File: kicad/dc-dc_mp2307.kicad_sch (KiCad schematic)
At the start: 20 parts

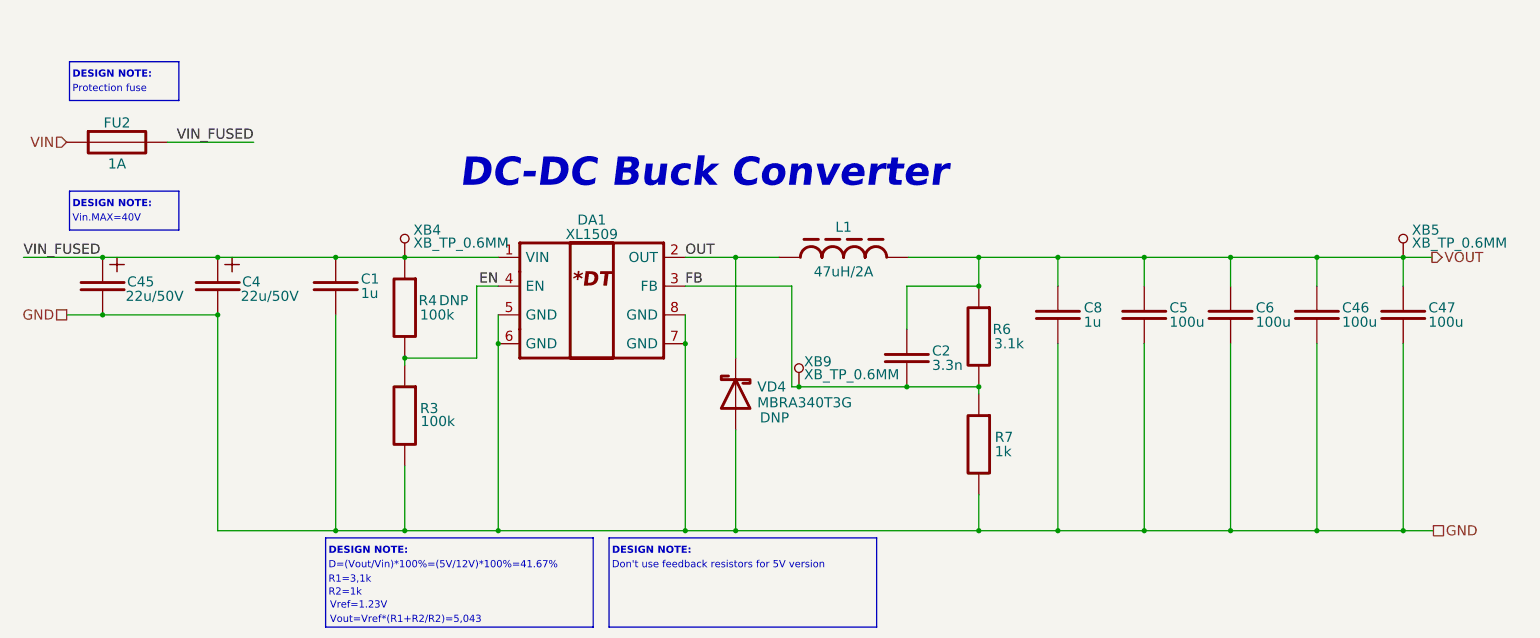
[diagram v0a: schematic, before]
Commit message: Reannotate schematic; Fix 5032 crystal footprint field; Update PCB with 5032 crystal
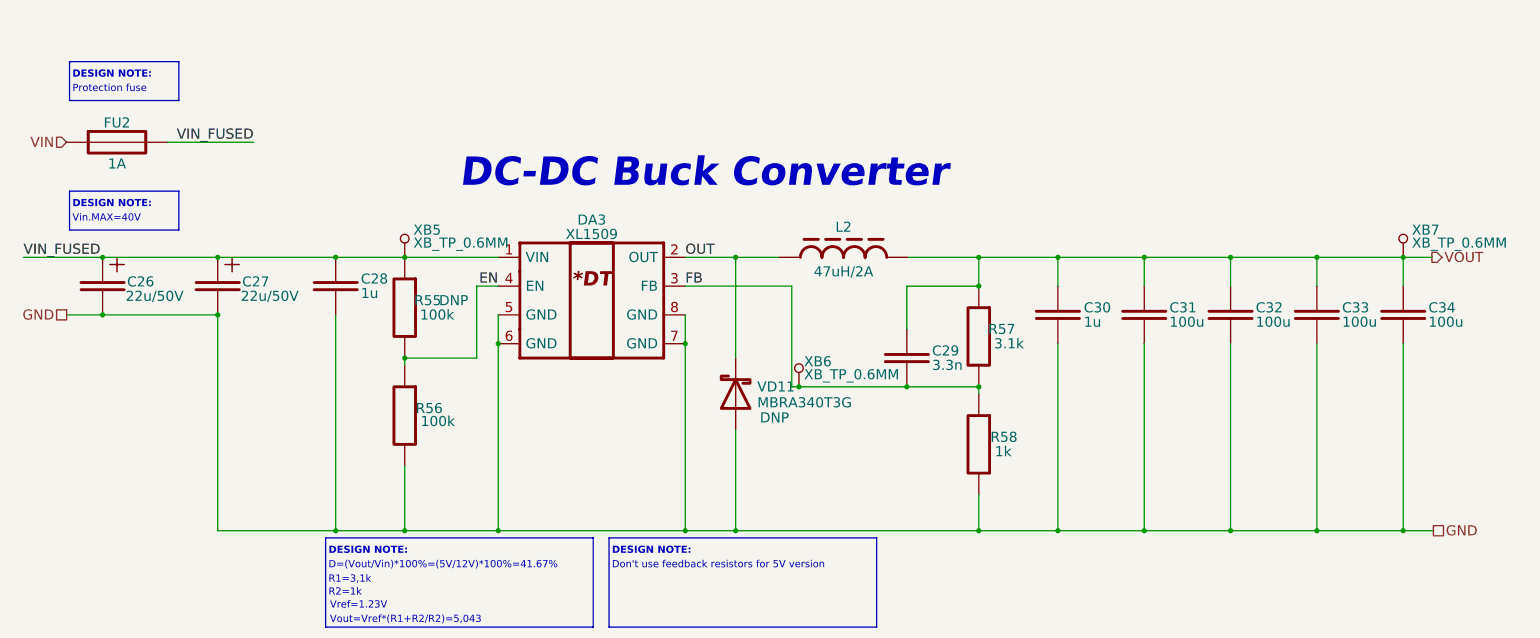
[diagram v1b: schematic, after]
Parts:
- renumbered C45 to C26, C4 to C27, C1 to C28, C2 to C29, C8 to C30, C5 to C31, C6 to C32, C46 to C33, C47 to C34, DA1 to DA3, L1 to L2, R4 to R55, R3 to R56, R6 to R57, R7 to R58, VD4 to VD11, XB4 to XB5, XB9 to XB6, XB5 to XB7
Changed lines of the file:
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@@
   (symbol (lib_id "Capacitors:C_CAP") (at 251.46 80.01 270) (unit 1)
     (in_bom yes) (on_board yes)
-    (property "Reference" "C46" (id 0) (at 255.905 78.74 90)
+    (property "Reference" "C33" (id 0) (at 255.905 78.74 90)
       (effects (font (size 1.778 1.778)) (justify left))
     )
@@
   (symbol (lib_id "Chips:XL1509") (at 123.444 77.47 0) (unit 1)
     (in_bom yes) (on_board yes)
-    (property "Reference" "DA1" (id 0) (at 123.444 63.246 0)
+    (property "Reference" "DA3" (id 0) (at 123.444 63.246 0)
       (effects (font (size 1.778 1.778)))
     )
@@
   (symbol (lib_id "Capacitors:C_CAP") (at 179.07 87.63 270) (unit 1)
     (in_bom yes) (on_board yes)
-    (property "Reference" "C2" (id 0) (at 183.515 86.36 90)
+    (property "Reference" "C29" (id 0) (at 183.515 86.36 90)
       (effects (font (size 1.778 1.778)) (justify left))
     )
@@
   (symbol (lib_id "Connectors:XB_TP_0.6MM") (at 160.0199 92.71 0) (unit 1)
     (in_bom no) (on_board yes)
-    (property "Reference" "XB9" (id 0) (at 160.909 88.265 0)
+    (property "Reference" "XB6" (id 0) (at 160.909 88.265 0)
       (effects (font (size 1.778 1.778)) (justify left))
     )
@@
   (symbol (lib_id "Diodes:VD_SCHOTTKY") (at 148.844 93.98 90) (unit 1)
     (in_bom yes) (on_board yes)
-    (property "Reference" "VD4" (id 0) (at 152.654 92.71 90)
+    (property "Reference" "VD11" (id 0) (at 152.654 92.71 90)
       (effects (font (size 1.778 1.778)) (justify right))
     )
@@
   (symbol (lib_id "Connectors:XB_TP_0.6MM") (at 266.7 69.85 0) (unit 1)
     (in_bom no) (on_board yes)
-    (property "Reference" "XB5" (id 0) (at 268.224 65.024 0)
+    (property "Reference" "XB7" (id 0) (at 268.224 65.024 0)
       (effects (font (size 1.778 1.778)) (justify left))
     )
@@
   (symbol (lib_id "Resistors:R_RES") (at 191.77 102.87 270) (unit 1)
     (in_bom yes) (on_board yes)
-    (property "Reference" "R7" (id 0) (at 196.215 101.6 90)
+    (property "Reference" "R58" (id 0) (at 196.215 101.6 90)
       (effects (font (size 1.778 1.778)))
     )
@@
   (symbol (lib_id "Resistors:R_RES") (at 90.424 78.74 270) (unit 1)
     (in_bom yes) (on_board yes)
-    (property "Reference" "R4" (id 0) (at 94.488 77.47 90)
+    (property "Reference" "R55" (id 0) (at 94.488 77.47 90)
       (effects (font (size 1.778 1.778)))
     )
@@
   (symbol (lib_id "Capacitors:C_CAP_PLUS") (at 57.404 74.93 270) (unit 1)
     (in_bom yes) (on_board yes)
-    (property "Reference" "C4" (id 0) (at 61.722 74.168 90)
+    (property "Reference" "C27" (id 0) (at 61.722 74.168 90)
       (effects (font (size 1.778 1.778)) (justify left))
     )
@@
   (symbol (lib_id "Capacitors:C_CAP") (at 220.98 80.01 270) (unit 1)
     (in_bom yes) (on_board yes)
-    (property "Reference" "C5" (id 0) (at 225.425 78.74 90)
+    (property "Reference" "C31" (id 0) (at 225.425 78.74 90)
       (effects (font (size 1.778 1.778)) (justify left))
     )
@@
   (symbol (lib_id "Capacitors:C_CAP") (at 78.232 74.93 270) (unit 1)
     (in_bom yes) (on_board yes)
-    (property "Reference" "C1" (id 0) (at 82.677 73.66 90)
+    (property "Reference" "C28" (id 0) (at 82.677 73.66 90)
       (effects (font (size 1.778 1.778)) (justify left))
     )
@@
   (symbol (lib_id "Capacitors:C_CAP") (at 266.7 80.01 270) (unit 1)
     (in_bom yes) (on_board yes)
-    (property "Reference" "C47" (id 0) (at 271.145 78.74 90)
+    (property "Reference" "C34" (id 0) (at 271.145 78.74 90)
       (effects (font (size 1.778 1.778)) (justify left))
     )
@@
   (symbol (lib_id "Capacitors:C_CAP_PLUS") (at 37.084 74.93 270) (unit 1)
     (in_bom yes) (on_board yes)
-    (property "Reference" "C45" (id 0) (at 41.402 74.168 90)
+    (property "Reference" "C26" (id 0) (at 41.402 74.168 90)
       (effects (font (size 1.778 1.778)) (justify left))
     )
@@
   (symbol (lib_id "Capacitors:C_CAP") (at 236.22 80.01 270) (unit 1)
     (in_bom yes) (on_board yes)
-    (property "Reference" "C6" (id 0) (at 240.665 78.74 90)
+    (property "Reference" "C32" (id 0) (at 240.665 78.74 90)
       (effects (font (size 1.778 1.778)) (justify left))
     )
@@
   (symbol (lib_id "Resistors:R_RES") (at 191.77 83.82 270) (unit 1)
     (in_bom yes) (on_board yes)
-    (property "Reference" "R6" (id 0) (at 195.834 82.55 90)
+    (property "Reference" "R57" (id 0) (at 195.834 82.55 90)
       (effects (font (size 1.778 1.778)))
     )
@@
   (symbol (lib_id "Inductors:L_DIEL") (at 167.894 69.85 0) (unit 1)
     (in_bom yes) (on_board yes)
-    (property "Reference" "L1" (id 0) (at 167.894 64.516 0)
+    (property "Reference" "L2" (id 0) (at 167.894 64.516 0)
       (effects (font (size 1.778 1.778)))
     )
@@
   (symbol (lib_id "Resistors:R_RES") (at 90.424 97.79 270) (unit 1)
     (in_bom yes) (on_board yes)
-    (property "Reference" "R3" (id 0) (at 94.742 96.52 90)
+    (property "Reference" "R56" (id 0) (at 94.742 96.52 90)
       (effects (font (size 1.778 1.778)))
     )
@@
   (symbol (lib_id "Capacitors:C_CAP") (at 205.74 80.01 270) (unit 1)
     (in_bom yes) (on_board yes)
-    (property "Reference" "C8" (id 0) (at 210.312 78.74 90)
+    (property "Reference" "C30" (id 0) (at 210.312 78.74 90)
       (effects (font (size 1.778 1.778)) (justify left))
     )
@@
   (symbol (lib_id "Connectors:XB_TP_0.6MM") (at 90.424 69.85 0) (unit 1)
     (in_bom no) (on_board yes)
-    (property "Reference" "XB4" (id 0) (at 91.948 65.024 0)
-      (effects (font (size 1.778 1.778)) (justify left))
-    )
+    (property "Reference" "XB5" (id 0) (at 91.948 65.024 0)
+      (effects (font (size 1.778 1.778)) (justify left))
+    )

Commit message: Add voltage value to caps, update BOM, SCH, ASM
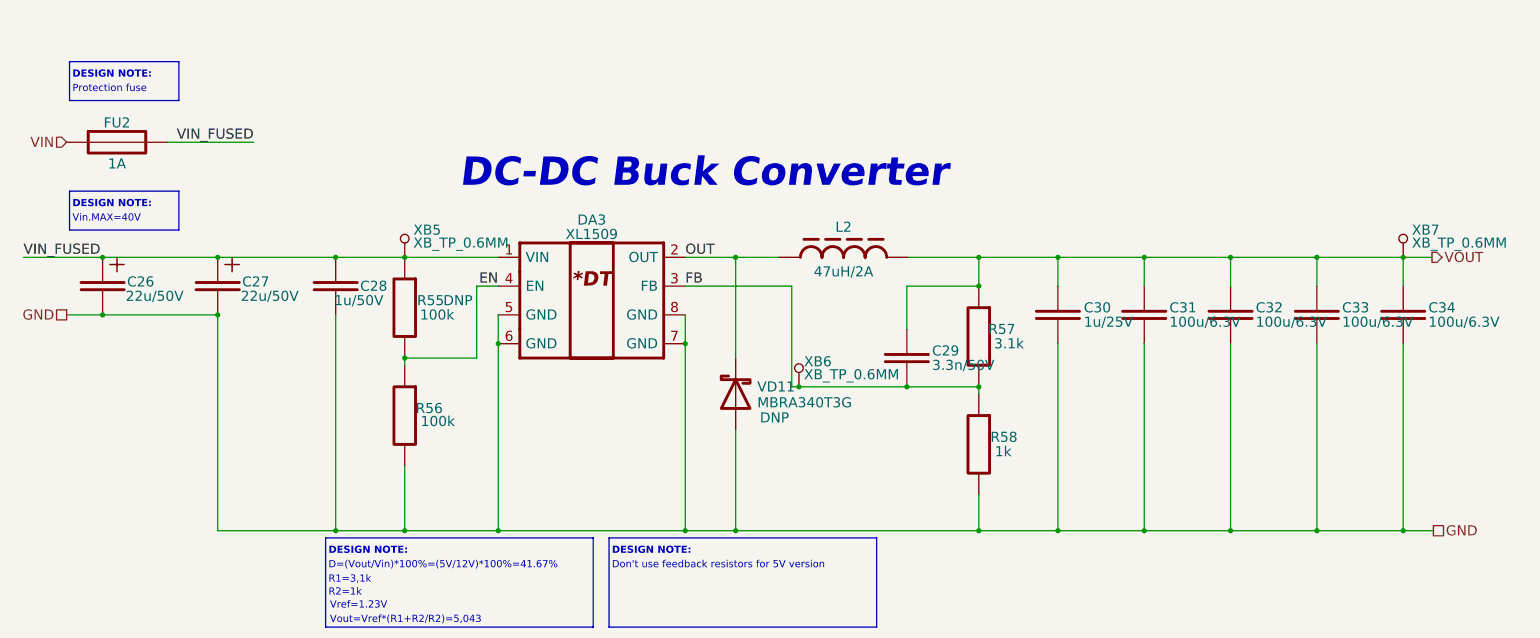
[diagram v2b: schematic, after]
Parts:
- C28: value 1u -> 1u/50V; Case/Package (none) -> 0805; Tolerance (none) -> ±10%; Type (none) -> X7R
- C29: value 3.3n -> 3.3n/50V; Case/Package (none) -> 1206; Tolerance (none) -> ±10%; Type (none) -> X7R
- C30: value 1u -> 1u/25V; Case/Package (none) -> 0603; Tolerance (none) -> ±10%; Type (none) -> X7R
- C31, C32, C33, C34: value 100u -> 100u/6.3V; Case/Package (none) -> 0603; Tolerance (none) -> ±10%; Type (none) -> X7R
- R55, R56: Case/Package 0000 -> 0603; Tolerance ±% -> ±5%
- R57: Case/Package 0000 -> 0603; Tolerance ±% -> ±1%
- R58: Case/Package 0000 -> 1206; Tolerance ±% -> ±1%

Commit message: Add docs; Update values of components according to PCB
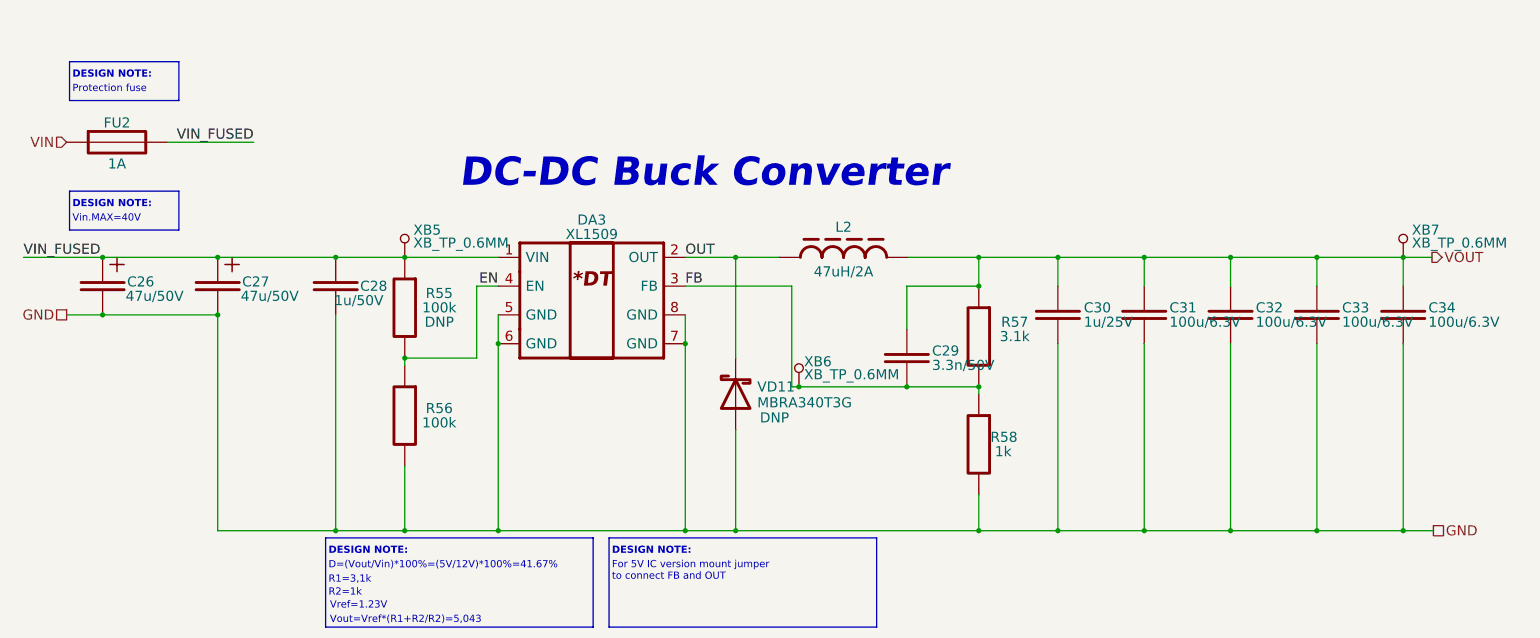
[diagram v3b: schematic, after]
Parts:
- C26, C27: value 22u/50V -> 47u/50V
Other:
- note added: "For 5V IC version mount jumper to connect FB and OUT"
- note removed: "Don't use feedback resistors for 5V version"
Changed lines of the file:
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@@
     (effects (font (size 1.27 1.27)) (justify left bottom))
   )
-  (text "Don't use feedback resistors for 5V version" (at 127 124.968 0)
+  (text "For 5V IC version mount jumper\nto connect FB and OUT"
+    (at 127 127 0)
     (effects (font (size 1.27 1.27)) (justify left bottom))
   )
@@
   (symbol (lib_name "R_RES_3") (lib_id "Resistors:R_RES") (at 90.424 78.74 270) (unit 1)
     (in_bom yes) (on_board yes)
-    (property "Reference" "R55" (id 0) (at 94.996 77.47 90)
-      (effects (font (size 1.778 1.778)))
-    )
-    (property "Value" "100k" (id 1) (at 96.139 80.01 90)
+    (property "Reference" "R55" (id 0) (at 96.52 76.2 90)
+      (effects (font (size 1.778 1.778)))
+    )
+    (property "Value" "100k" (id 1) (at 96.52 78.74 90)
       (effects (font (size 1.778 1.778)))
     )
@@
       (effects (font (size 1.778 1.778)) hide)
     )
-    (property "Assembly" "DNP" (id 4) (at 99.822 77.47 90)
+    (property "Assembly" "DNP" (id 4) (at 96.52 81.28 90)
       (effects (font (size 1.778 1.778)))
     )
@@
       (effects (font (size 1.778 1.778)) (justify left))
     )
-    (property "Value" "22u/50V" (id 1) (at 61.468 76.708 90)
+    (property "Value" "47u/50V" (id 1) (at 61.468 76.708 90)
       (effects (font (size 1.778 1.778)) (justify left))
     )
@@
       (effects (font (size 1.778 1.778)) (justify left))
     )
-    (property "Value" "22u/50V" (id 1) (at 41.148 76.708 90)
+    (property "Value" "47u/50V" (id 1) (at 41.148 76.708 90)
       (effects (font (size 1.778 1.778)) (justify left))
     )
@@
   (symbol (lib_name "R_RES_1") (lib_id "Resistors:R_RES") (at 191.77 83.82 270) (unit 1)
     (in_bom yes) (on_board yes)
-    (property "Reference" "R57" (id 0) (at 195.834 82.55 90)
-      (effects (font (size 1.778 1.778)))
-    )
-    (property "Value" "3.1k" (id 1) (at 197.104 85.09 90)
+    (property "Reference" "R57" (id 0) (at 198.12 81.28 90)
+      (effects (font (size 1.778 1.778)))
+    )
+    (property "Value" "3.1k" (id 1) (at 198.12 83.82 90)
       (effects (font (size 1.778 1.778)))
     )
@@
   (symbol (lib_id "Resistors:R_RES") (at 90.424 97.79 270) (unit 1)
     (in_bom yes) (on_board yes)
-    (property "Reference" "R56" (id 0) (at 94.742 96.52 90)
-      (effects (font (size 1.778 1.778)))
-    )
-    (property "Value" "100k" (id 1) (at 96.266 98.806 90)
-      (effects (font (size 1.778 1.778)))
-    )
+    (property "Reference" "R56" (id 0) (at 96.52 96.52 90)
+      (effects (font (size 1.778 1.778)))
+    )
+    (property "Value" "100k" (id 1) (at 96.52 99.06 90)
+      (effects (font (size 1.778 1.778)))
+    )
